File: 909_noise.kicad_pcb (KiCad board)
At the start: 2 copper layers, 30 x 20 mm, 18 parts, among them J1 Conn_01x02_Pin, J2 Conn_01x03_Pin, J3 Conn_ARM_JTAG_SWD_10, SW1 PTS645SM43SMTR92 LFS, U1 STM32G030J6Mx, U2 L78L33ABUTR, U3 TLV7211A

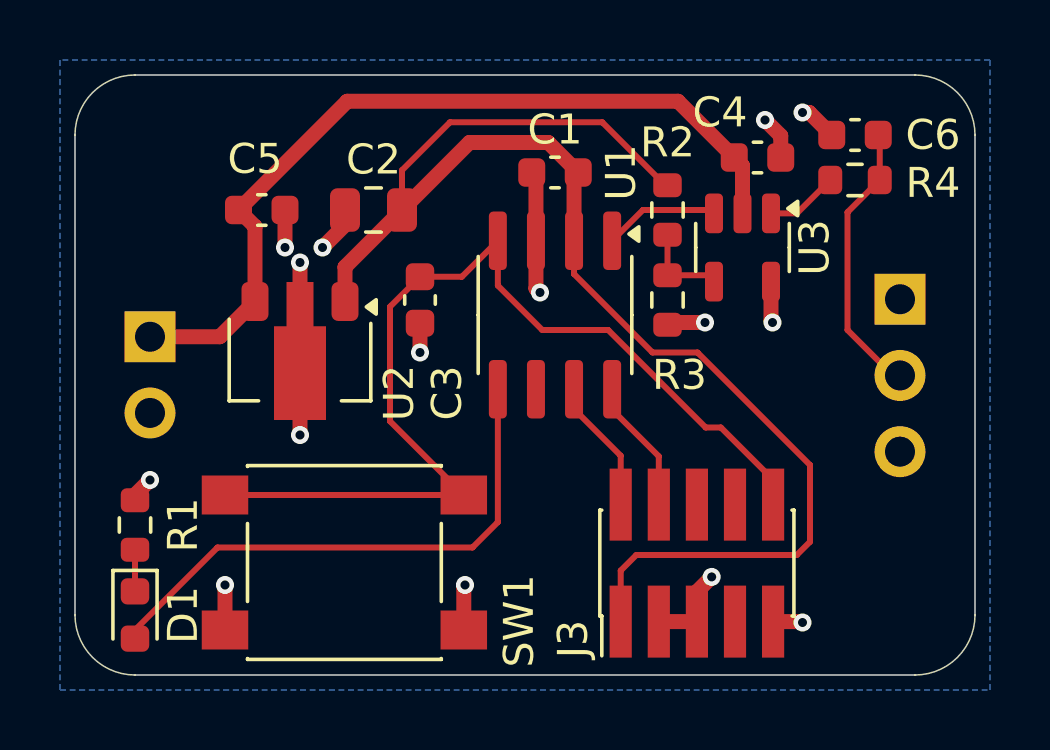
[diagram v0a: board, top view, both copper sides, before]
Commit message: add decals to back of board, rearrange silk slightly
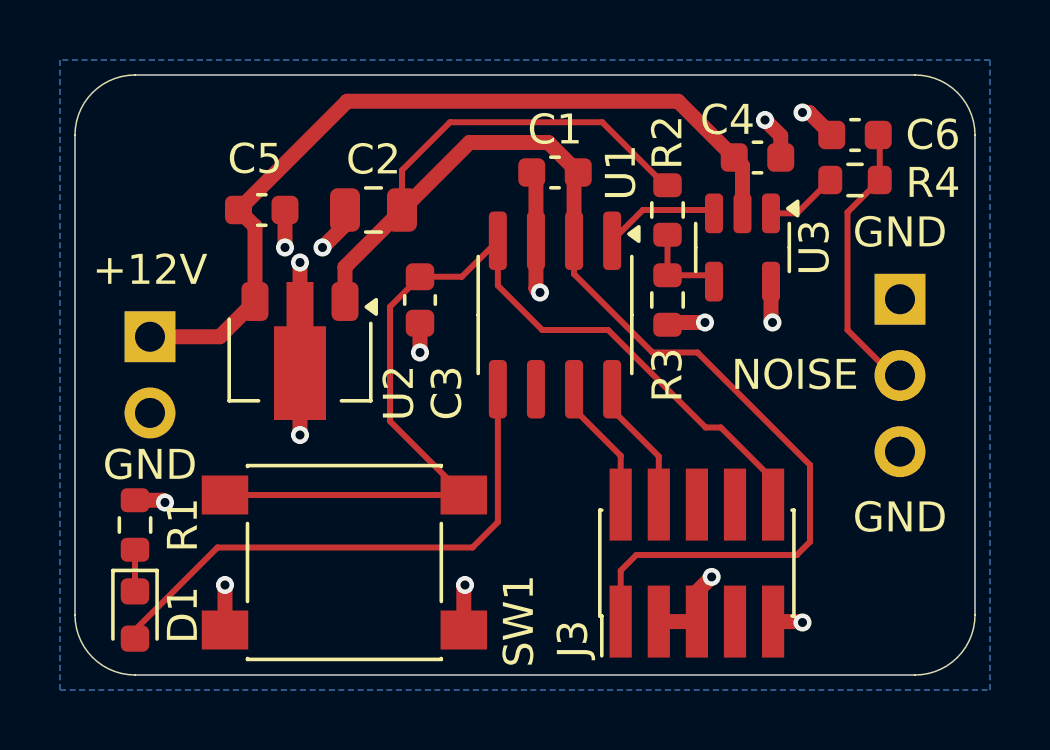
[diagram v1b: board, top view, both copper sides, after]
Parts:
- added LOGO1: CC-BY-SA_0.33in, Symbol_CreativeCommons:CC-BY-SA_SilkScreenTop_Small, B.Cu at (63.5, 30.8)
- added LOGO2: Logo_MadeWithKiCad, Symbol:KiCad-Logo2_5mm_SilkScreen, B.Cu at (63.5, 25.3)

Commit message: change to cheaper debug connector
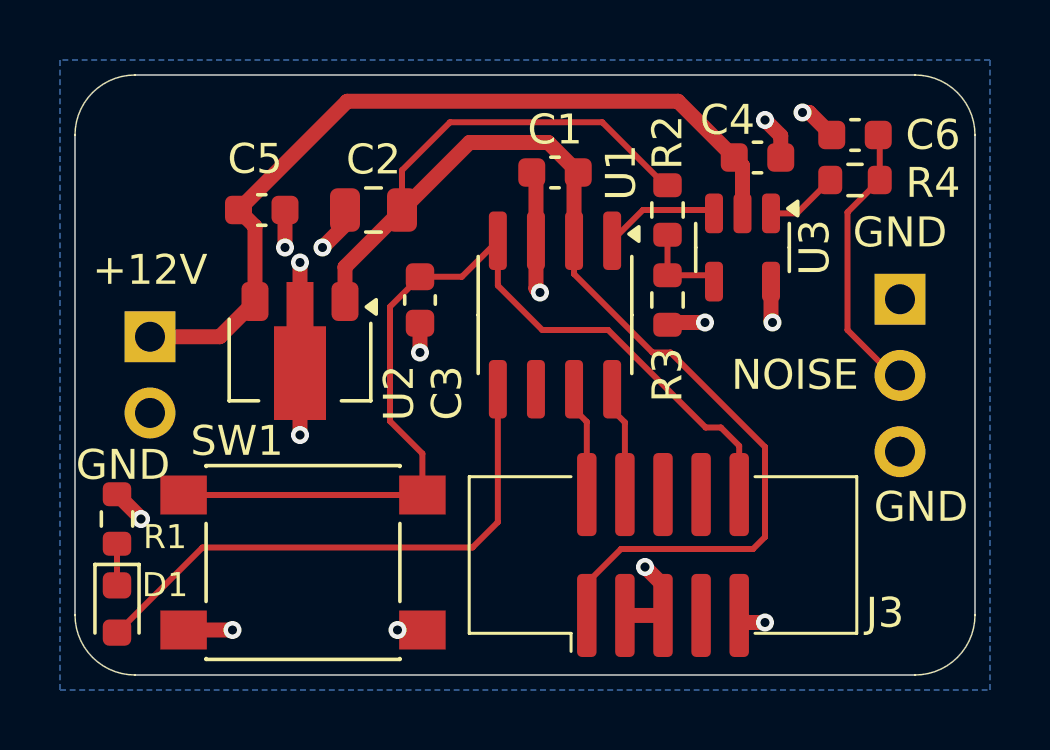
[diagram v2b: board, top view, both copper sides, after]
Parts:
- J3: value Conn_ARM_JTAG_SWD_10 -> 3220-10-0300-00; footprint Connector_PinHeader_1.27mm:PinHeader_2x05_P1.27mm_Vertical_SMD -> Connector_CNC_Tech:CNC_Tech_3220-10-0300-00_2x05_P1.27mm_Vertical
- moved SW1 1.38 mm to (52.6, 36.2)
- moved J3 1.16 mm to (64.6, 36.0)
- moved D1 0.63 mm to (46.4, 37.8)
- moved R1 0.63 mm to (46.4, 34.8)
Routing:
- net +3.3V: track 47.7 -> 45.6 mm
- net /~{reset}: track 33.9 -> 32.6 mm
- net /swdio: track 4.49 -> 3.69 mm
- net /swclk: track 4.49 -> 3.69 mm
